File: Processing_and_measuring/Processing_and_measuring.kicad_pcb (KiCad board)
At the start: 2 copper layers, 49 parts, among them J1 Conn_02x07_Counter_Clockwise, J2 Conn_01x02_Pin, J3 Conn_02x07_Counter_Clockwise, J4 Conn_01x04_Pin, J5 Conn_01x02_Pin, J6 Conn_01x02_Pin, U1 TPL7407LAD, U2 CD74HC4067M, U3 AVR128DA48x-xPT, U4 TPL7407LAD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

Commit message: Didn't save before last commit
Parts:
- removed J5: Conn_01x02_Pin, Connector_PinHeader_1.00mm:PinHeader_1x02_P1.00mm_Horizontal
- moved C3 57.9 mm to (168.5, 72.0)
- moved R18 5.43 mm to (172.7, 65.5), turned to 0 degrees
- moved C4 4.64 mm to (171.9, 67.9), turned to 90 degrees
- moved R20 1.99 mm to (175.2, 67.9), turned to 90 degrees
- moved R17 0.67 mm to (173.6, 67.9), turned to 90 degrees
- turned C5 to 0 degrees
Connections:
- J2 pad 2: VIN -> Power
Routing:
- net +5V: track 65.5 -> 120.9 mm, vias 0 -> 2
- net GND: track 31.0 -> 39.7 mm, vias 9 -> 10
- net Net-(VR1-EN): track 5.55 -> 10.2 mm, vias 0 -> 2
- net Net-(VR1-FB): track 2.76 -> 5.35 mm

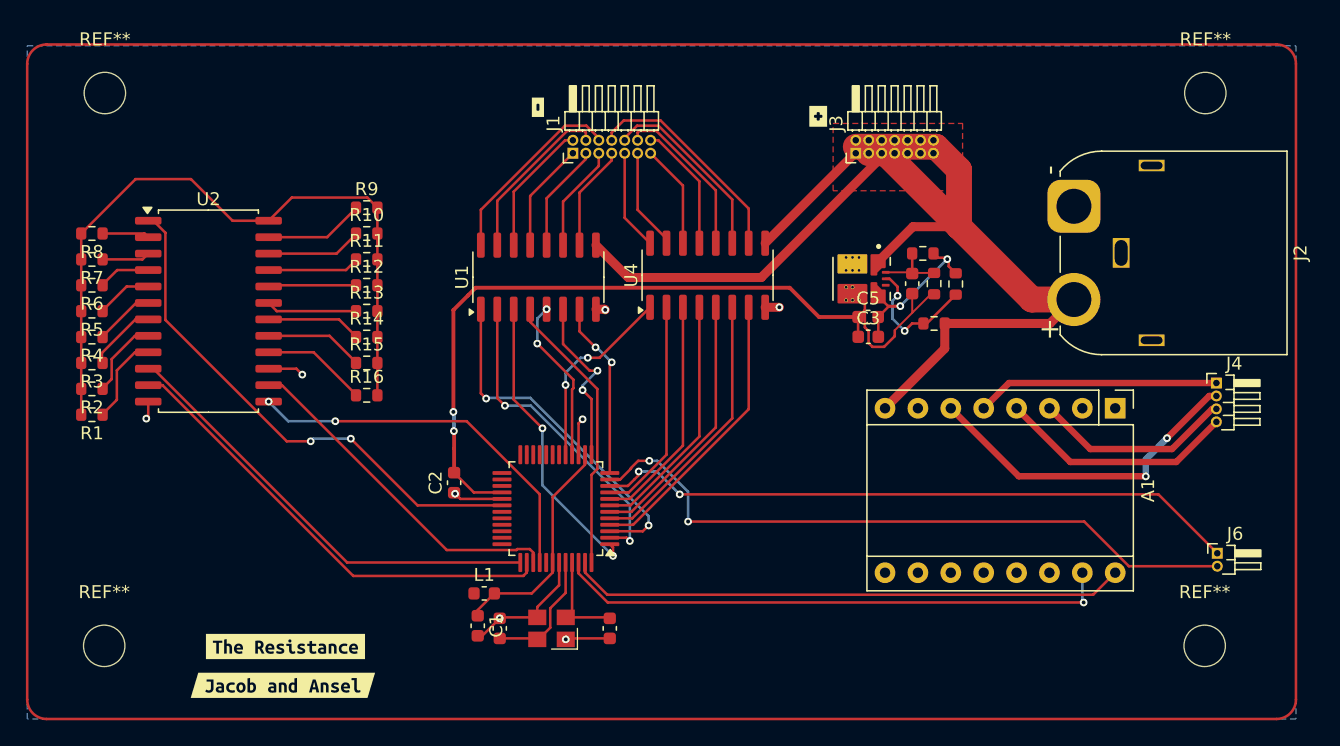
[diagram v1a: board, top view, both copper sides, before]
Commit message: added button to mcu
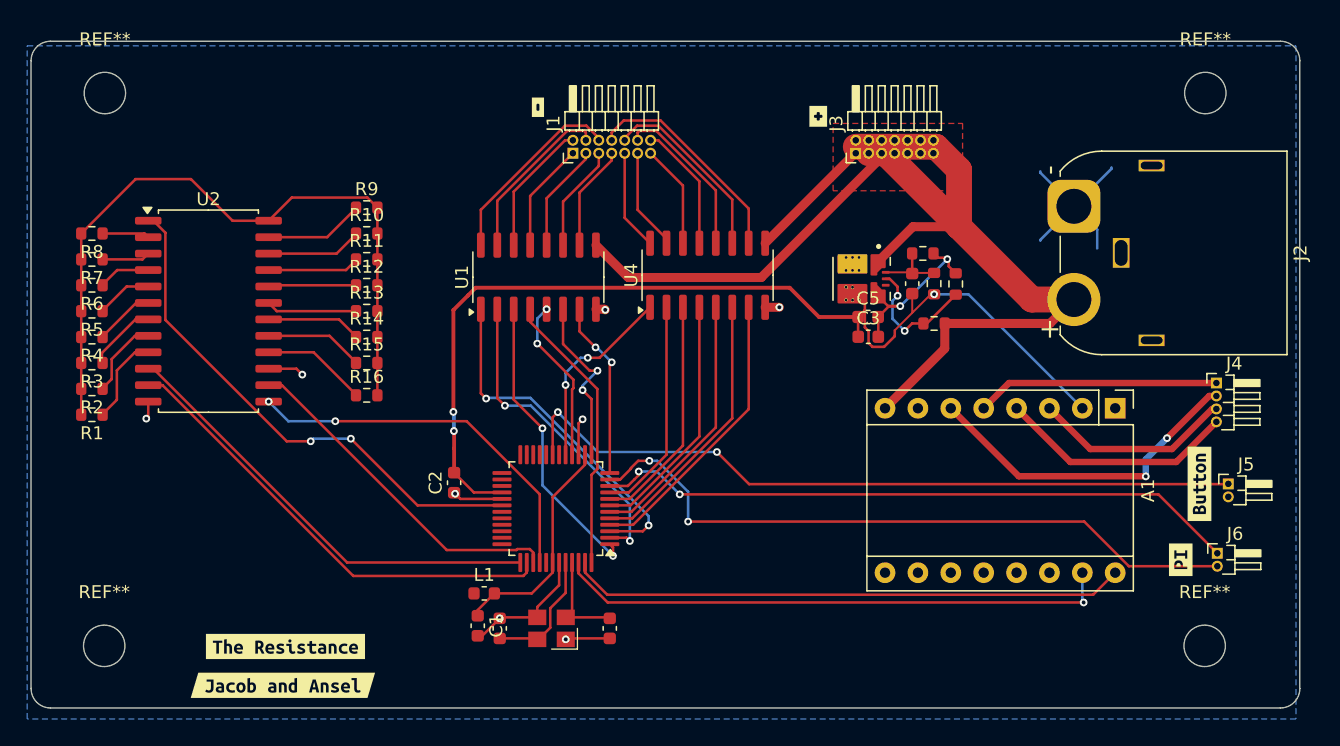
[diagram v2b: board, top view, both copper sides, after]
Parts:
- added J5: Conn_01x02_Pin, Connector_PinHeader_1.00mm:PinHeader_1x02_P1.00mm_Horizontal, F.Cu at (196.3, 83.3)
- added kibuzzard-6920EC74: G***, kibuzzard-6920EC74, F.Cu at (194.1, 83.3)
- added kibuzzard-6920EC8A: G***, kibuzzard-6920EC8A, F.Cu at (192.6, 89.2)
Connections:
- U3 pad 19: unconnected-(U3-PC7-Pad19) -> /button
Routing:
- net /button: track 0.00 -> 57.6 mm, vias 0 -> 2
- net GND: track 39.7 -> 55.4 mm
- net +5V: track 120.9 -> 136.0 mm, vias 2 -> 3
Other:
- board outline added: 98 x 51.5 mm

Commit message: Fixing errors and warnings
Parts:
- J1, J3: footprint Connector_PinHeader_1.00mm:PinHeader_2x07_P1.00mm_Horizontal -> Connector_PinHeader_2.54mm:PinHeader_2x07_P2.54mm_Vertical
- J4: footprint Connector_PinHeader_1.00mm:PinHeader_1x04_P1.00mm_Horizontal -> Connector_PinHeader_2.54mm:PinHeader_1x04_P2.54mm_Vertical
- J5, J6: footprint Connector_PinHeader_1.00mm:PinHeader_1x02_P1.00mm_Horizontal -> Connector_PinHeader_2.54mm:PinHeader_1x02_P2.54mm_Vertical
- moved kibuzzard-6920EC74 12.2 mm to (199.5, 94.3)
- moved J3 7.55 mm to (160.0, 59.0)
- moved J1 6.80 mm to (139.0, 59.0)
- moved kibuzzard-6920EC8A 4.27 mm to (190.9, 93.1)
- moved J5 4.20 mm to (198.6, 86.8)
- moved kibuzzard-6920BB24 3.42 mm to (167.7, 53.5)
- moved J4 3.16 mm to (198.5, 75.6)
- moved kibuzzard-6920BB03 2.55 mm to (145.5, 53.8)
- moved J6 1.96 mm to (194.2, 90.2), turned to -90 degrees
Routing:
- net +5V: track 136.0 -> 172.8 mm, vias 3 -> 5
- net Power: track 134.4 -> 125.3 mm
- net Net-(J1-Pin_8): track 17.1 -> 22.9 mm
- net Net-(J1-Pin_10): track 14.6 -> 18.9 mm
- net /button: track 57.6 -> 61.3 mm
- net /RXD: track 52.3 -> 48.7 mm
- net /5: track 18.8 -> 21.9 mm
- net Net-(J1-Pin_6): track 15.1 -> 18.2 mm
- net /4: track 18.4 -> 20.9 mm
- net Net-(J1-Pin_13): track 7.99 -> 5.72 mm
- net Net-(J1-Pin_12): track 12.7 -> 14.9 mm
- net Net-(J1-Pin_7): track 8.13 -> 6.03 mm
- net Net-(J1-Pin_5): track 8.24 -> 6.20 mm
- net Net-(J1-Pin_4): track 13.2 -> 15.2 mm
- net /3: track 15.5 -> 17.4 mm
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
